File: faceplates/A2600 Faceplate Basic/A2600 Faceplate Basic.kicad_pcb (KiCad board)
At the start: 2 copper layers, 61 x 99.7 mm, 7 parts, among them M1 Mounting, M2 Mounting, M3 Mounting, M4 Mounting

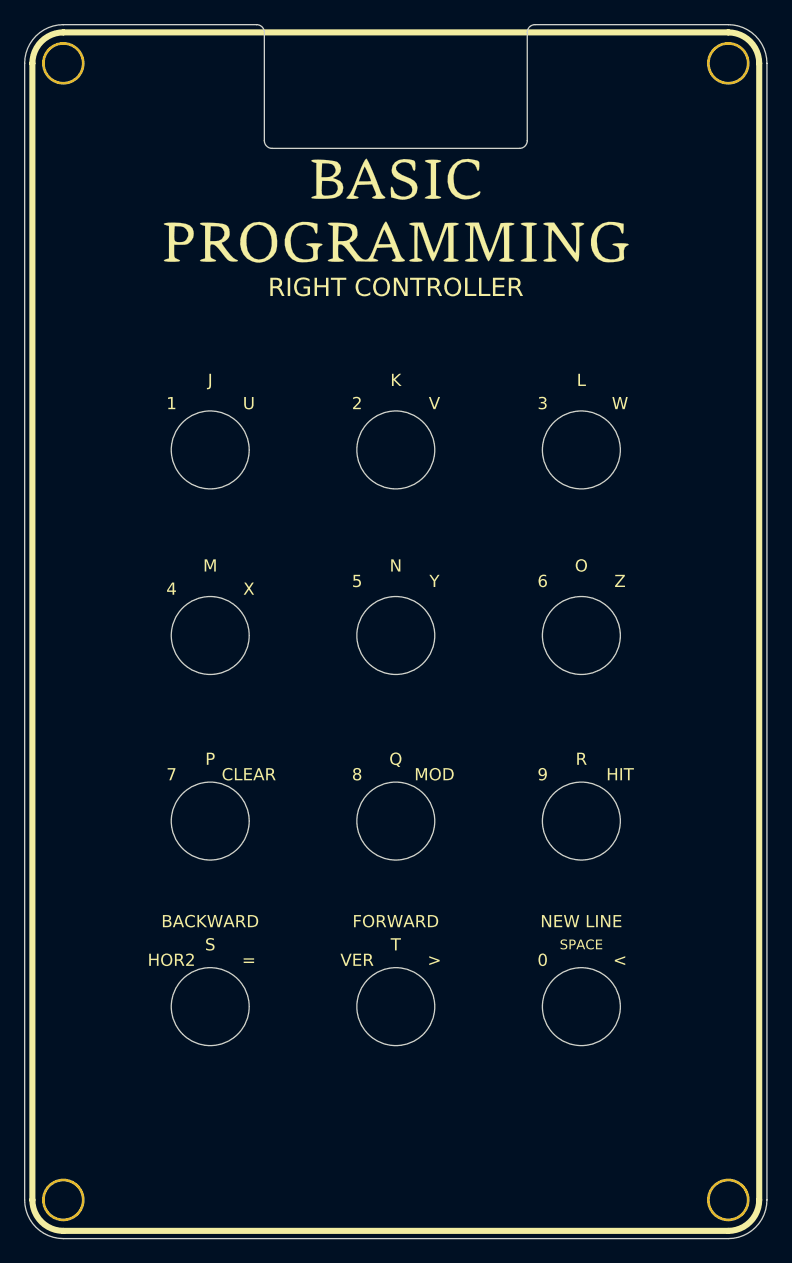
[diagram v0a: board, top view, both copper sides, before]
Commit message: Tweaked basic faceplate and added images
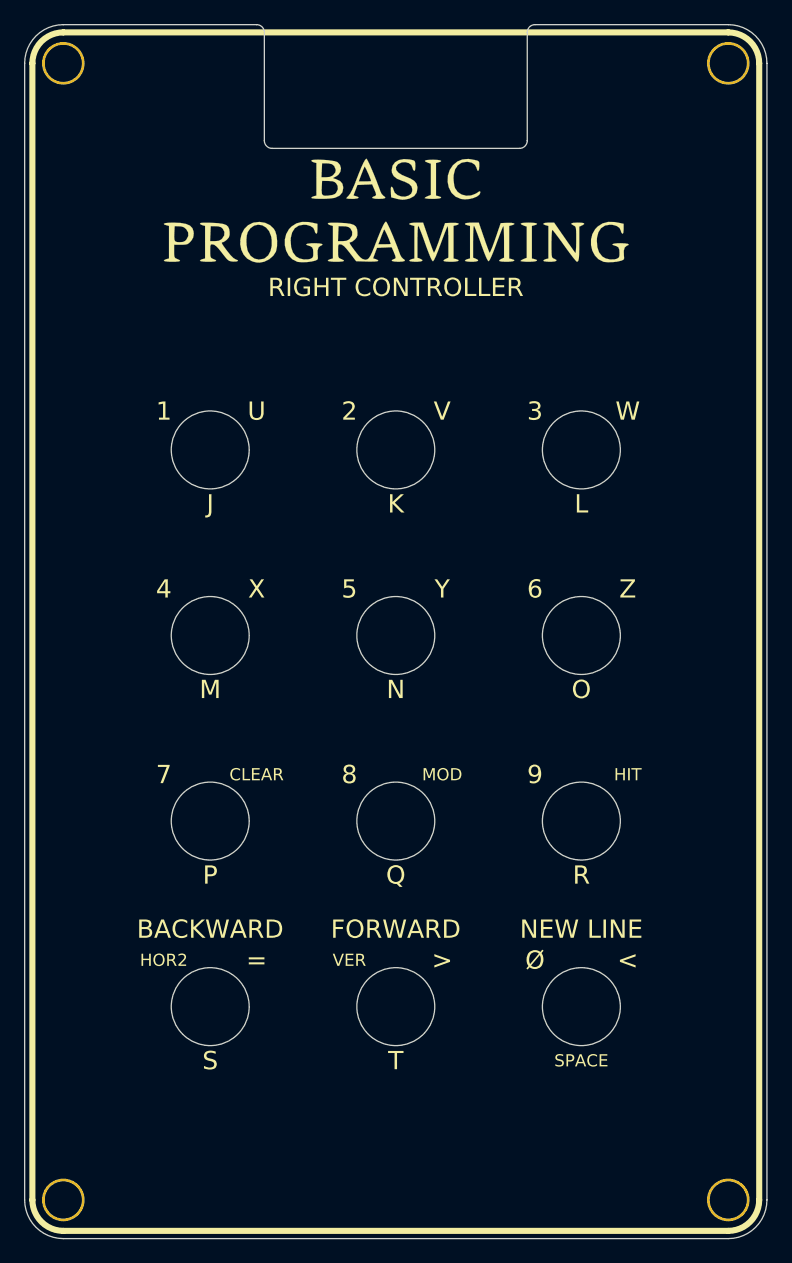
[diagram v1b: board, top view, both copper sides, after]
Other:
- board text added: "A"
- board text added: "Ø"
- board text removed: "0"
